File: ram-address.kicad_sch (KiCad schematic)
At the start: 35 parts, among them SW3 SW_DIP_x08, U22 74HCT157, U23 74HCT157, U8 74HCT173, U9 74HCT173

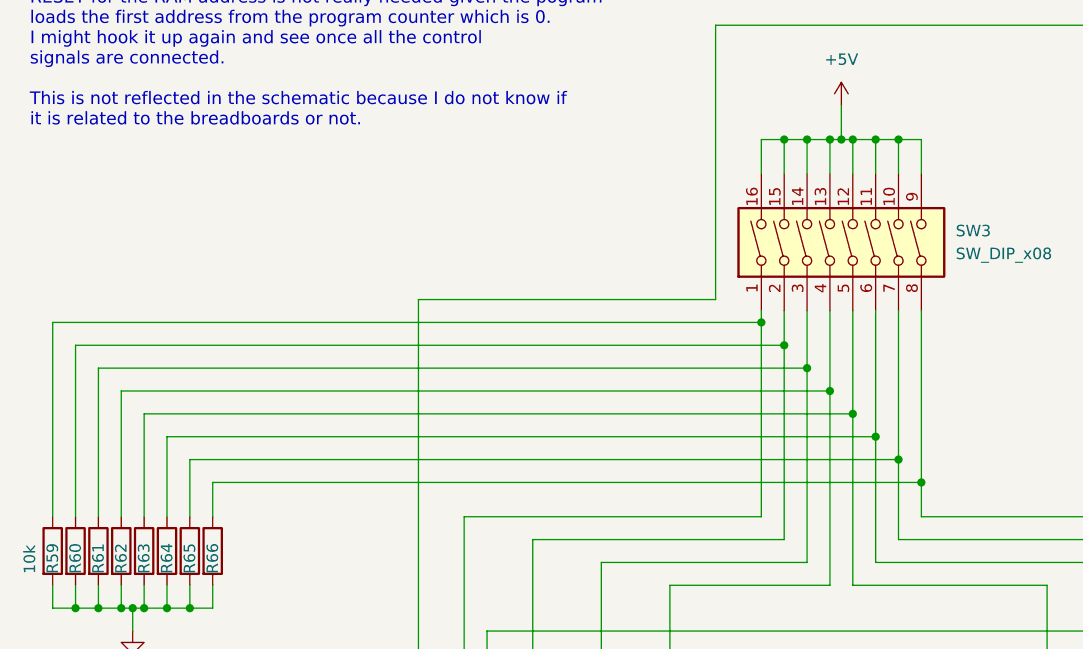
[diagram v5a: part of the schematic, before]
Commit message: add arduino headers for programming
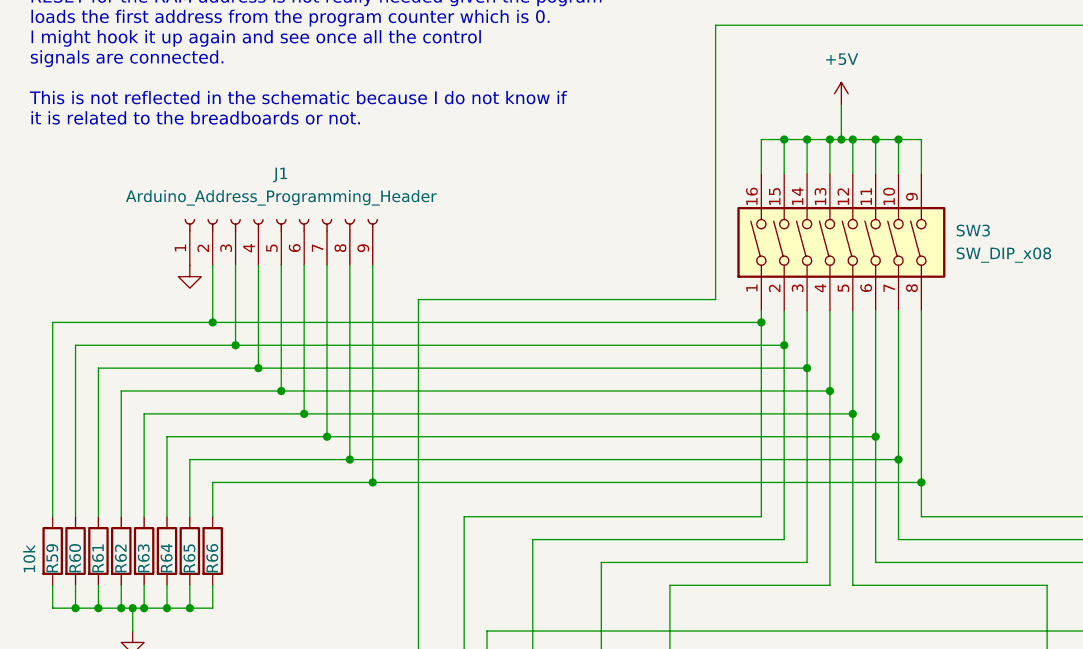
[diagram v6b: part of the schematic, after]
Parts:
- added J1: Arduino_Address_Programming_Header, Connector_PinSocket_2.54mm:PinSocket_1x09_P2.54mm_Vertical, symbol Connector:Conn_01x09_Socket
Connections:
- net GND: now also J1.1 (Pin_1)
- net at R59.1, SW3.1, U22.13 (4B): now also J1.2 (Pin_2)
- net at R60.1, SW3.2, U22.10 (3B): now also J1.3 (Pin_3)
- net at R61.1, SW3.3, U22.6 (2B): now also J1.4 (Pin_4)
- net at R62.1, SW3.4, U22.3 (1B): now also J1.5 (Pin_5)
- net at R63.1, SW3.5, U23.13 (4B): now also J1.6 (Pin_6)
- net at R64.1, SW3.6, U23.10 (3B): now also J1.7 (Pin_7)
- net at R65.1, SW3.7, U23.6 (2B): now also J1.8 (Pin_8)
- net at R66.1, SW3.8, U23.3 (1B): now also J1.9 (Pin_9)
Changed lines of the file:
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@@
   (junction (at 87.63 161.29) (diameter 0) (color 0 0 0 0)
   )
+  (junction (at 44.45 81.28) (diameter 0) (color 0 0 0 0)
+  )
   (junction (at 97.79 73.66) (diameter 0) (color 0 0 0 0)
   )
+  (junction (at 34.29 71.12) (diameter 0) (color 0 0 0 0)
+  )
   (junction (at 95.25 193.04) (diameter 0) (color 0 0 0 0)
   )
@@
   (junction (at 160.02 134.62) (diameter 0) (color 0 0 0 0)
   )
+  (junction (at 41.91 78.74) (diameter 0) (color 0 0 0 0)
+  )
   (junction (at 190.5 66.04) (diameter 0) (color 0 0 0 0)
   )
@@
   (junction (at 125.73 193.04) (diameter 0) (color 0 0 0 0)
   )
+  (junction (at 52.07 88.9) (diameter 0) (color 0 0 0 0)
+  )
   (junction (at 95.25 71.12) (diameter 0) (color 0 0 0 0)
   )
+  (junction (at 46.99 83.82) (diameter 0) (color 0 0 0 0)
+  )
   (junction (at 95.25 134.62) (diameter 0) (color 0 0 0 0)
   )
+  (junction (at 49.53 86.36) (diameter 0) (color 0 0 0 0)
+  )
   (junction (at 105.41 193.04) (diameter 0) (color 0 0 0 0)
   )
@@
   (junction (at 74.93 193.04) (diameter 0) (color 0 0 0 0)
   )
+  (junction (at 39.37 76.2) (diameter 0) (color 0 0 0 0)
+  )
   (junction (at 21.59 102.87) (diameter 0) (color 0 0 0 0)
   )
@@
   )
   (junction (at 104.14 50.8) (diameter 0) (color 0 0 0 0)
+  )
+  (junction (at 36.83 73.66) (diameter 0) (color 0 0 0 0)
   )
   (junction (at 144.78 69.85) (diameter 0) (color 0 0 0 0)
@@
     (stroke (width 0) (type default))
   )
+  (wire (pts (xy 49.53 64.77) (xy 49.53 86.36))
+    (stroke (width 0) (type default))
+  )
   (wire (pts (xy 110.49 69.85) (xy 110.49 86.36))
     (stroke (width 0) (type default))
@@
     (stroke (width 0) (type default))
   )
+  (wire (pts (xy 39.37 76.2) (xy 100.33 76.2))
+    (stroke (width 0) (type default))
+  )
   (wire (pts (xy 160.02 134.62) (xy 160.02 138.43))
     (stroke (width 0) (type default))
@@
     (stroke (width 0) (type default) (color 0 0 255 1))
   )
-  (wire (pts (xy 26.67 81.28) (xy 105.41 81.28))
+  (wire (pts (xy 46.99 83.82) (xy 107.95 83.82))
+    (stroke (width 0) (type default))
+  )
+  (wire (pts (xy 26.67 81.28) (xy 44.45 81.28))
     (stroke (width 0) (type default))
   )
@@
     (stroke (width 0) (type default))
   )
-  (wire (pts (xy 24.13 78.74) (xy 102.87 78.74))
+  (wire (pts (xy 44.45 64.77) (xy 44.45 81.28))
+    (stroke (width 0) (type default))
+  )
+  (wire (pts (xy 41.91 64.77) (xy 41.91 78.74))
+    (stroke (width 0) (type default))
+  )
+  (wire (pts (xy 24.13 78.74) (xy 41.91 78.74))
     (stroke (width 0) (type default))
   )
@@
     (stroke (width 0) (type default) (color 255 0 0 1))
   )
+  (wire (pts (xy 39.37 64.77) (xy 39.37 76.2))
+    (stroke (width 0) (type default))
+  )
   (wire (pts (xy 125.73 172.72) (xy 125.73 175.26))
     (stroke (width 0) (type default))
@@
     (stroke (width 0) (type default))
   )
-  (wire (pts (xy 16.51 71.12) (xy 95.25 71.12))
-    (stroke (width 0) (type default))
-  )
   (wire (pts (xy 129.54 151.13) (xy 129.54 158.75))
     (stroke (width 0) (type default))
   )
   (wire (pts (xy 229.87 53.34) (xy 229.87 57.15))
+    (stroke (width 0) (type default))
+  )
+  (wire (pts (xy 16.51 71.12) (xy 34.29 71.12))
     (stroke (width 0) (type default))
   )
@@
     (stroke (width 0) (type default) (color 255 0 0 1))
   )
+  (wire (pts (xy 34.29 71.12) (xy 95.25 71.12))
+    (stroke (width 0) (type default))
+  )
   (wire (pts (xy 102.87 50.8) (xy 102.87 54.61))
     (stroke (width 0) (type default))
@@
     (stroke (width 0) (type default))
   )
-  (wire (pts (xy 21.59 76.2) (xy 100.33 76.2))
+  (wire (pts (xy 49.53 86.36) (xy 110.49 86.36))
+    (stroke (width 0) (type default))
+  )
+  (wire (pts (xy 36.83 64.77) (xy 36.83 73.66))
+    (stroke (width 0) (type default))
+  )
+  (wire (pts (xy 21.59 76.2) (xy 39.37 76.2))
     (stroke (width 0) (type default))
   )
@@
     (stroke (width 0) (type default))
   )
-  (wire (pts (xy 29.21 83.82) (xy 107.95 83.82))
+  (wire (pts (xy 29.21 83.82) (xy 46.99 83.82))
     (stroke (width 0) (type default))
   )
@@
     (stroke (width 0) (type default) (color 0 0 255 1))
   )
+  (wire (pts (xy 52.07 88.9) (xy 113.03 88.9))
+    (stroke (width 0) (type default))
+  )
   (wire (pts (xy 261.62 139.7) (xy 182.88 139.7))
     (stroke (width 0) (type default))
@@
     (stroke (width 0) (type default))
   )
+  (wire (pts (xy 36.83 73.66) (xy 97.79 73.66))
+    (stroke (width 0) (type default))
+  )
   (wire (pts (xy 95.25 193.04) (xy 95.25 190.5))
     (stroke (width 0) (type default))
@@
     (stroke (width 0) (type default))
   )
+  (wire (pts (xy 52.07 64.77) (xy 52.07 88.9))
+    (stroke (width 0) (type default))
+  )
   (wire (pts (xy 190.5 66.04) (xy 190.5 69.85))
     (stroke (width 0) (type default))
@@
   )
   (wire (pts (xy 43.18 171.45) (xy 64.77 171.45))
+    (stroke (width 0) (type default))
+  )
+  (wire (pts (xy 41.91 78.74) (xy 102.87 78.74))
     (stroke (width 0) (type default))
   )
@@
     (stroke (width 0) (type default))
   )
+  (wire (pts (xy 34.29 64.77) (xy 34.29 71.12))
+    (stroke (width 0) (type default))
+  )
   (wire (pts (xy 95.25 71.12) (xy 95.25 92.71))
     (stroke (width 0) (type default))
@@
     (stroke (width 0) (type default))
   )
-  (wire (pts (xy 31.75 86.36) (xy 110.49 86.36))
+  (wire (pts (xy 31.75 86.36) (xy 49.53 86.36))
     (stroke (width 0) (type default))
   )
@@
     (stroke (width 0) (type default))
   )
-  (wire (pts (xy 34.29 88.9) (xy 113.03 88.9))
+  (wire (pts (xy 34.29 88.9) (xy 52.07 88.9))
     (stroke (width 0) (type default))
   )
@@
     (stroke (width 0) (type default) (color 255 0 0 1))
   )
+  (wire (pts (xy 46.99 64.77) (xy 46.99 83.82))
+    (stroke (width 0) (type default))
+  )
   (wire (pts (xy 261.62 21.59) (xy 245.11 21.59))
     (stroke (width 0) (type default) (color 0 0 255 1))
@@
     (stroke (width 0) (type default))
   )
-  (wire (pts (xy 19.05 73.66) (xy 97.79 73.66))
+  (wire (pts (xy 19.05 73.66) (xy 36.83 73.66))
     (stroke (width 0) (type default))
   )
@@
   )
   (wire (pts (xy 54.61 193.04) (xy 64.77 193.04))
+    (stroke (width 0) (type default))
+  )
+  (wire (pts (xy 44.45 81.28) (xy 105.41 81.28))
     (stroke (width 0) (type default))
   )
@@
     )
   )
+  (symbol (lib_id "power:GND") (at 31.75 64.77 0) (unit 1)
+    (in_bom yes) (on_board yes) (dnp no) (fields_autoplaced)
+    (property "Reference" "#PWR0251" (at 31.75 71.12 0)
+      (effects (font (size 1.27 1.27)) hide)
+    )
+    (property "Value" "GND" (at 31.75 69.85 0)
+      (effects (font (size 1.27 1.27)) hide)
+    )
+    (property "Footprint" "" (at 31.75 64.77 0)
+      (effects (font (size 1.27 1.27)) hide)
+    )
+    (property "Datasheet" "" (at 31.75 64.77 0)
+      (effects (font (size 1.27 1.27)) hide)
+    )
+    (pin "1")
+    (instances
+      (project "8-bit-cpu"
+        (path "/100bb8d1-c3d6-4e1f-87b6-72e4e187243c/33b906b8-f63f-4a46-8ef2-4150917936b8/b8600875-f531-45d3-8c06-c8d636c0c136"
+          (reference "#PWR0251") (unit 1)
+        )
+      )
+    )
+  )
   (symbol (lib_id "power:GND") (at 100.33 193.04 0) (unit 1)
     (in_bom yes) (on_board yes) (dnp no) (fields_autoplaced)
@@
         )
       )
+    )
+  )
+  (symbol (lib_id "Connector:Conn_01x09_Socket") (at 41.91 59.69 90) (unit 1)
+    (in_bom yes) (on_board yes) (dnp no) (fields_autoplaced)
+    (property "Reference" "J1" (at 41.91 54.61 90)
+      (effects (font (size 1.27 1.27)))
+    )
+    (property "Value" "Arduino_Address_Programming_Header" (at 41.91 57.15 90)
+      (effects (font (size 1.27 1.27)))
+    )
+    (property "Footprint" "Connector_PinSocket_2.54mm:PinSocket_1x09_P2.54mm_Vertical" (at 41.91 59.69 0)
+      (effects (font (size 1.27 1.27)) hide)
+    )
+    (property "Datasheet" "~" (at 41.91 59.69 0)
+      (effects (font (size 1.27 1.27)) hide)
+    )
+    (pin "1")
+    (pin "4")
+    (pin "6")
+    (pin "5")
+    (pin "3")
+    (pin "7")
+    (pin "9")
+    (pin "2")
+    (pin "8")
+    (instances
+      (project "8-bit-cpu"
+        (path "/100bb8d1-c3d6-4e1f-87b6-72e4e187243c/33b906b8-f63f-4a46-8ef2-4150917936b8/b8600875-f531-45d3-8c06-c8d636c0c136"
+          (reference "J1") (unit 1)
+        )
+      )

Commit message: trying to solve issues
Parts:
- added C27: 10n, symbol Device:C
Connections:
- net GND: now also C27.2
- net RESET: now also C27.1
